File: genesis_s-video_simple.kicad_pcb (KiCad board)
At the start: 2 copper layers, 34 x 17.8 mm, 12 parts, among them J1 Y In, J2 C In, J3 +5V, J4 Y Out, J5 C Out, J6 GND, J7 CGND, J8 YGND, Q2 KSC945

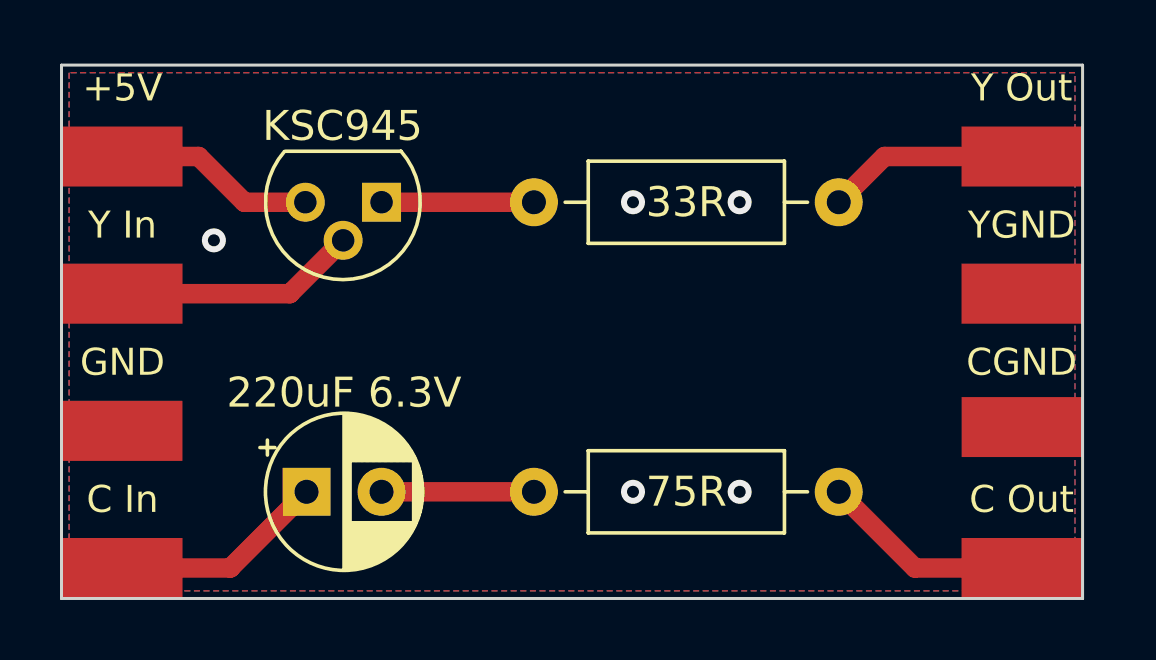
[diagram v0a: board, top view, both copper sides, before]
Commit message: minor update
slightly shrunk pcb, widened transistor pins for easier installation, and slight silkscreen change
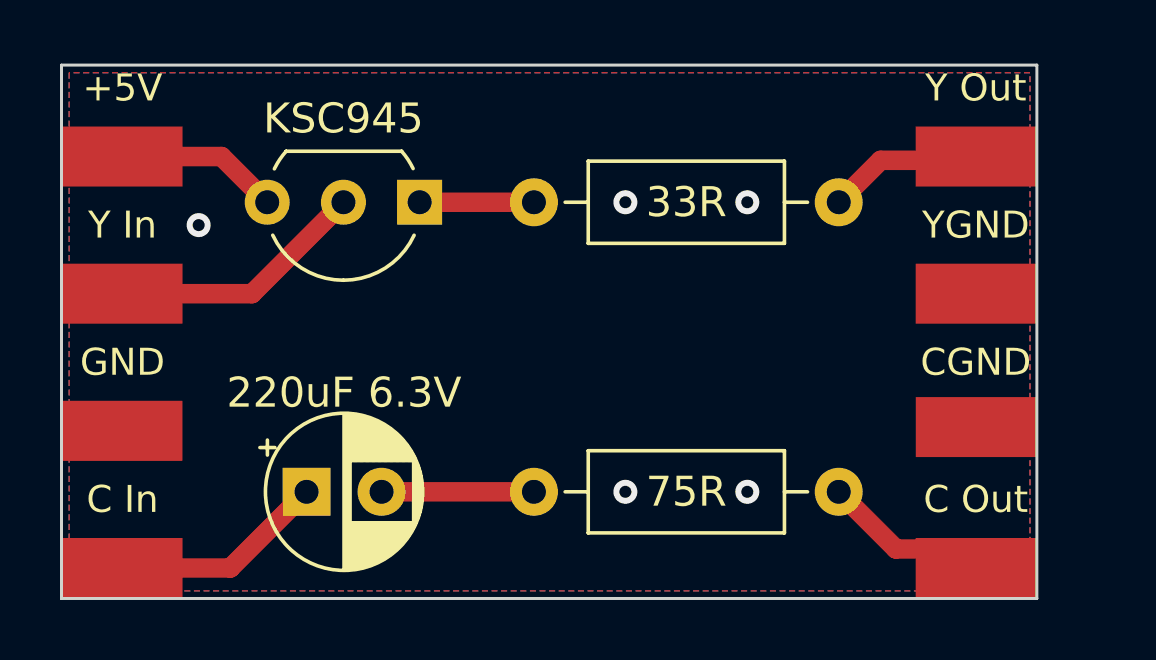
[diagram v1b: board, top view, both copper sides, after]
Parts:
- Q1: renamed from Q2; footprint Package_TO_SOT_THT:TO-92L -> Package_TO_SOT_THT:TO-92L_Inline_Wide
- moved J7 1.53 mm to (136.1, 88.3)
- moved J4 1.53 mm to (136.1, 79.2)
- moved J5 1.53 mm to (136.1, 93.0)
- moved J8 1.53 mm to (136.1, 83.8)
- moved Q1 1.27 mm to (117.6, 80.8)
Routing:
- net Net-(J5-Pin_1): track 7.15 -> 5.62 mm
- net Net-(J4-Pin_1): track 6.73 -> 5.20 mm
- net Net-(Q2-E): track 5.08 -> 3.81 mm
- net +5V: track 6.73 -> 5.46 mm
- net Net-(J1-Pin_1): track 8.09 -> 8.63 mm
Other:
- board size 34 x 17.8 mm -> 32.5 x 17.8 mm
